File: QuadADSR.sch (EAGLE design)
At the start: 61 parts, among them IC1 74AC32D, IC5 MCP6004D, Q1 20MHz, T1 2N3904, T2 2N3904, T3 2N3904, T4 2N3904, U1 ATMEGA328P, U2 DUAL_OPAMP, U3 7805

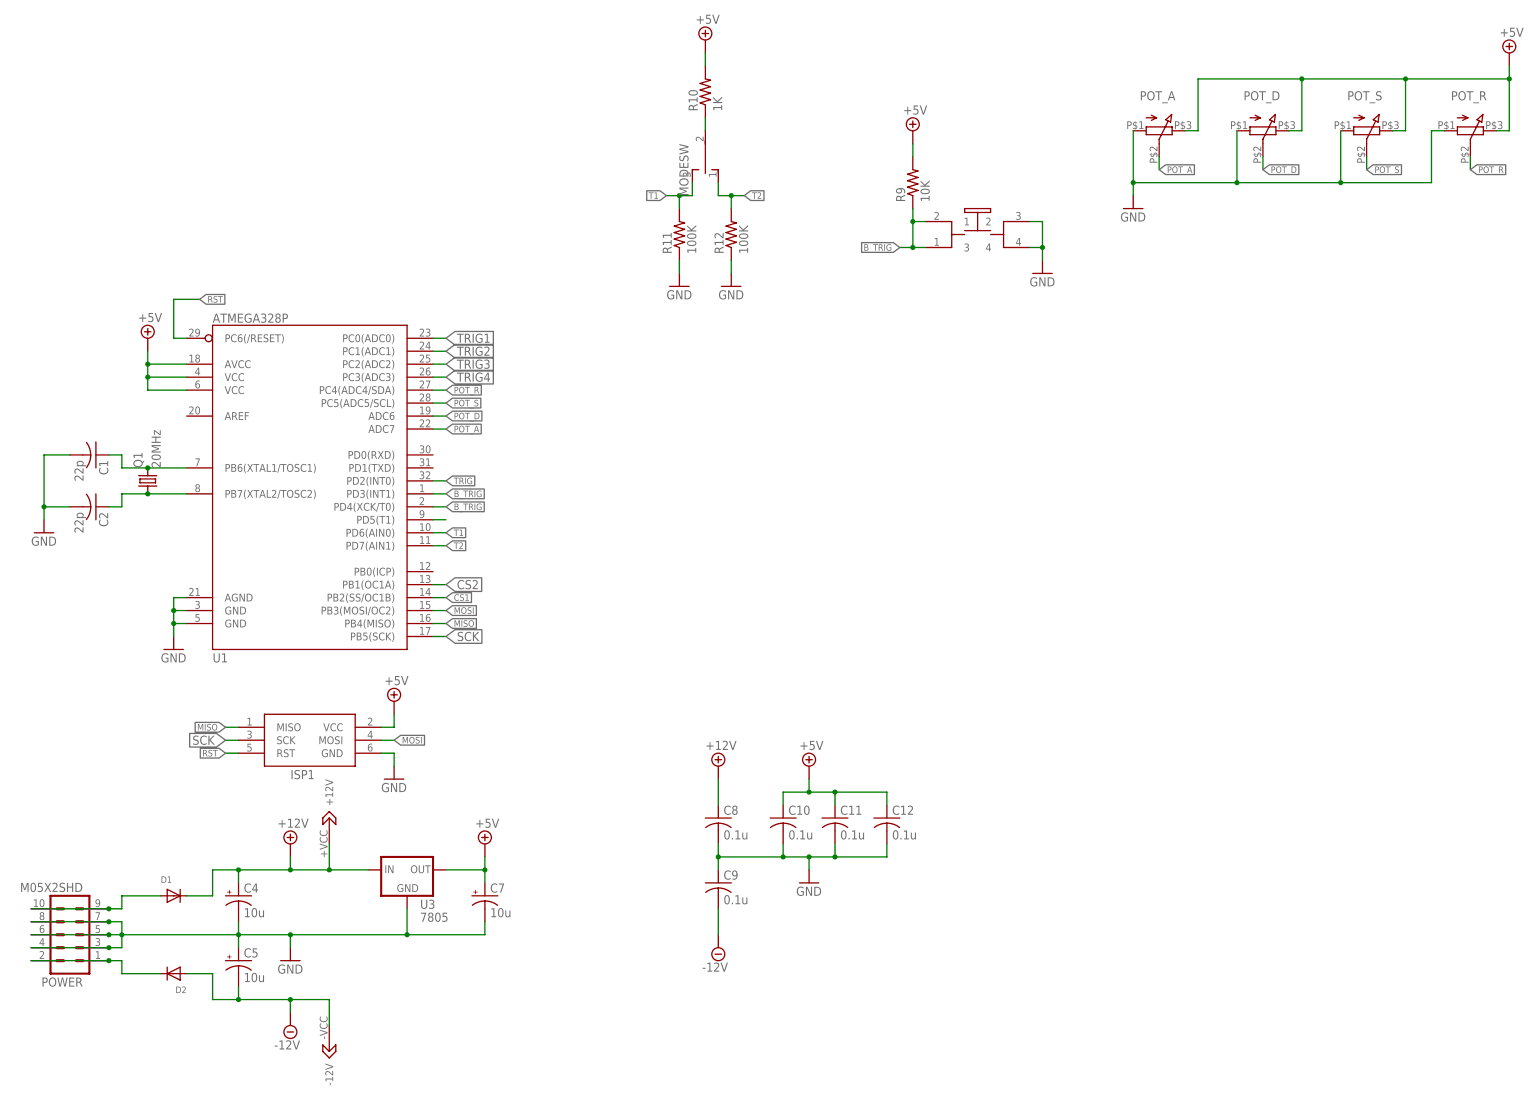
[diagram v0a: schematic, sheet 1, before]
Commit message: Layed out board with shape pots
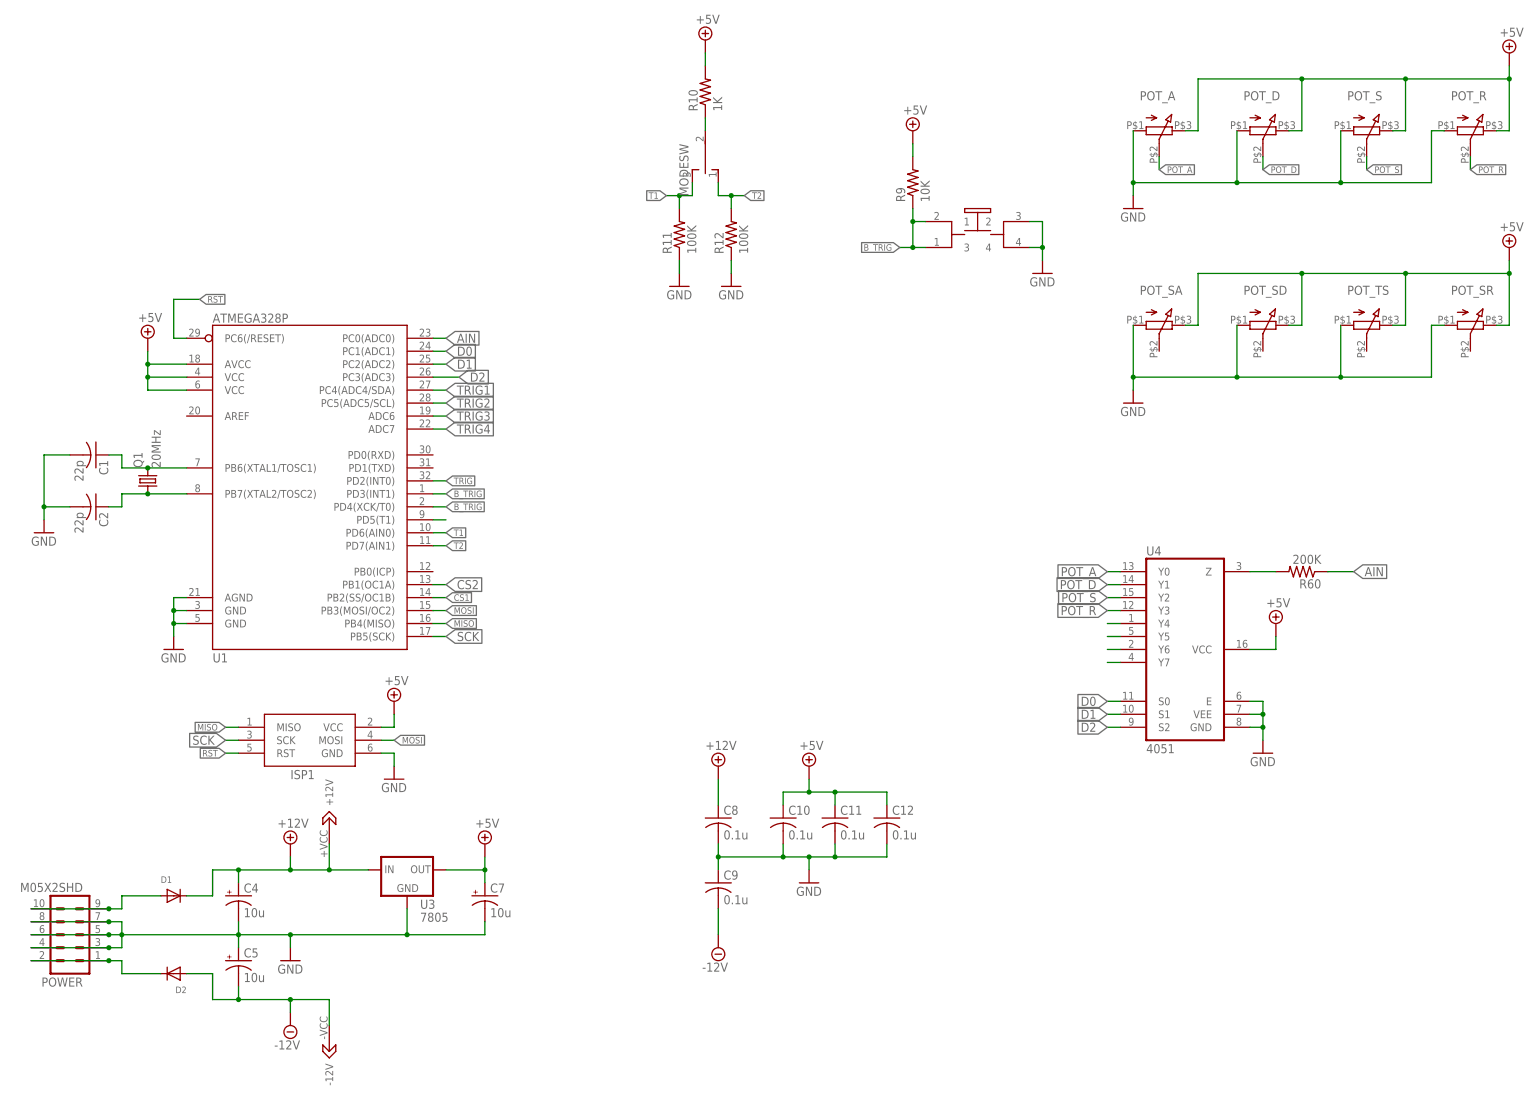
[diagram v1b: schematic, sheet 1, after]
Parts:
- added POT_SA, POT_SD, POT_SR, POT_TS: Q-POT, INSTRUO:Q-POT
- added R60: 200K, rcl:R-US_R0805
- added U4: 4051, INSTRUO:MUX!
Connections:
- new net AIN: R60.1, U1.PC0(ADC0)
- new net D0: U1.PC1(ADC1), U4.S0
- new net D1: U1.PC2(ADC2), U4.S1
- new net D2: U1.PC3(ADC3), U4.S2
- new net N$23: U4.Y4
- new net N$24: U4.Y5
- new net N$26: U4.Y6
- new net N$27: U4.Y7
- new net N$69: R60.2, U4.Z
- net +5V: now also POT_SA.3, POT_SD.3, POT_SR.3, POT_TS.3, U4.VCC
- net GND: now also POT_SA.1, POT_SD.1, POT_SR.1, POT_TS.1, U4.E, U4.GND, U4.VEE
- net POT_A: now also U4.Y0
- net POT_D: now also U4.Y1
- net POT_R: now also U4.Y3
- net POT_S: now also U4.Y2
- net TRIG1: now also U1.PC4(ADC4/SDA); no longer U1.PC0(ADC0)
- net TRIG2: now also U1.PC5(ADC5/SCL); no longer U1.PC1(ADC1)
- net TRIG3: now also U1.ADC6; no longer U1.PC2(ADC2)
- net TRIG4: now also U1.ADC7; no longer U1.PC3(ADC3)

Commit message: Moved a few thigs round
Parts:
- removed BUT: PB6149L-5, INSTRUO:PB6149L-5
- removed POT_TS: Q-POT, INSTRUO:Q-POT
- added D3: Red, led:LED5MM
- added D4: Green, led:LED5MM
- added D5: BLue, led:LED5MM
- added D6: Yellow, led:LED5MM
- added POT_ST: Q-POT, INSTRUO:Q-POT
- added R17, R18, R19: (no value), resistor:R-EU_R0805
- R9: value 10K -> (none); device rcl:R-US_R0805 -> resistor:R-EU_R0805
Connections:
- removed net B_TRIG: BUTG$1.1, BUTG$1.3, R9.1, U1.PD3(INT1), U1.PD4(XCK/T0)
- removed net D0: U1.PC1(ADC1), U4.S0
- removed net D1: U1.PC2(ADC2), U4.S1
- removed net D2: U1.PC3(ADC3), U4.S2
- removed net N$23: U4.Y4
- removed net N$24: U4.Y5
- removed net N$26: U4.Y6
- removed net N$27: U4.Y7
- new net LED_A: R9.2, U1.PD0(RXD)
- new net LED_B: R17.2, U1.PD1(TXD)
- new net LED_C: R18.2, U1.PD3(INT1)
- new net LED_D: R19.2, U1.PD4(XCK/T0)
- new net N$19: D3.A, R9.1
- new net N$20: D4.A, R17.1
- new net N$21: D5.A, R18.1
- new net N$22: D6.A, R19.1
- new net POT_SA: POT_SA.2, U4.Y4
- new net POT_SD: POT_SD.2, U4.Y5
- new net POT_SR: POT_SR.2, U4.Y7
- new net POT_ST: POT_ST.2, U4.Y6
- new net S0: U1.PC0(ADC0), U4.S0
- new net S1: U1.PC1(ADC1), U4.S1
- new net S2: U1.PC2(ADC2), U4.S2
- net +5V: now also POT_ST.3; no longer POT_TS.3, R9.2
- net AIN: now also U1.PC3(ADC3); no longer U1.PC0(ADC0)
- net GND: now also D3.C, D4.C, D5.C, D6.C, POT_ST.1; no longer BUTG$1.2, BUTG$1.4, POT_TS.1
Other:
- moved on the sheet: POT_SA, POT_SD, POT_SR, R60, U4

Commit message: Moved a few thigs round
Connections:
- removed net 3VREF: U$3.VREFA, U$3.VREFB, U$4.VREFA, U$4.VREFB
- removed net N$16: IC1P.GND
- removed net N$17: IC1P.VCC
- net +5V: now also C15.1, IC1P.VCC, IC5P.V+, U$3.VDD, U$3.VREFA, U$3.VREFB, U$4.VDD, U$4.VREFA, U$4.VREFB, U$4.~SHDN
- net 5V: no longer C15.1, IC5P.V+, U$3.VDD, U$4.VDD, U$4.~SHDN
- net GND: now also IC1P.GND
- net TRIG: no longer U1.PD5(T1)
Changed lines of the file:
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@@
 <part name="SUPPLY17" library="supply2" deviceset="+5V" device=""/>
 <part name="R60" library="rcl" deviceset="R-US_" device="R0805" value="200K"/>
+<part name="SUPPLY18" library="supply2" library_urn="urn:adsk.eagle:library:372" deviceset="+5V" device=""/>
+<part name="SUPPLY19" library="supply2" library_urn="urn:adsk.eagle:library:372" deviceset="+5V" device=""/>
+<part name="SUPPLY20" library="supply2" library_urn="urn:adsk.eagle:library:372" deviceset="+5V" device=""/>
+<part name="SUPPLY21" library="supply2" library_urn="urn:adsk.eagle:library:372" deviceset="+5V" device=""/>
+<part name="SUPPLY22" library="supply2" library_urn="urn:adsk.eagle:library:372" deviceset="+5V" device=""/>
+<part name="SUPPLY23" library="supply2" library_urn="urn:adsk.eagle:library:372" deviceset="+5V" device=""/>
 </parts>
 <sheets>
@@
 <junction x="25.4" y="-27.94"/>
 <pinref part="U3" gate="G$1" pin="GND"/>
-<wire x1="60.96" y1="-25.4" x2="83.82" y2="-25.4" width="0.1524" layer="91"/>
+<wire x1="60.96" y1="-25.4" x2="71.12" y2="-25.4" width="0.1524" layer="91"/>
+<wire x1="71.12" y1="-25.4" x2="83.82" y2="-25.4" width="0.1524" layer="91"/>
 <wire x1="83.82" y1="-25.4" x2="83.82" y2="-20.32" width="0.1524" layer="91"/>
 <junction x="60.96" y="-25.4"/>
@@
 <wire x1="99.06" y1="-25.4" x2="99.06" y2="-22.86" width="0.1524" layer="91"/>
 <junction x="83.82" y="-25.4"/>
+<wire x1="71.12" y1="-25.4" x2="71.12" y2="-30.48" width="0.1524" layer="91"/>
+<junction x="71.12" y="-25.4"/>
+<label x="73.66" y="-30.48" size="1.778" layer="95"/>
 </segment>
 <segment>
@@
 <wire x1="99.06" y1="-10.16" x2="99.06" y2="-12.7" width="0.1524" layer="91"/>
 <junction x="99.06" y="-12.7"/>
+<wire x1="99.06" y1="-12.7" x2="104.14" y2="-12.7" width="0.1524" layer="91"/>
+<label x="106.68" y="-12.7" size="1.778" layer="95"/>
 </segment>
 <segment>
@@
 </net>
 <net name="TRIG" class="0">
-<segment>
-<pinref part="U1" gate="G$1" pin="PD5(T1)"/>
-<wire x1="88.9" y1="55.88" x2="91.44" y2="55.88" width="0.1524" layer="91"/>
-</segment>
 <segment>
 <pinref part="U1" gate="G$1" pin="PD2(INT0)"/>
@@
 <instance part="C16" gate="G$1" x="7.62" y="71.12"/>
 <instance part="C17" gate="G$1" x="17.78" y="71.12"/>
+<instance part="SUPPLY18" gate="+5V" x="-10.16" y="124.46"/>
+<instance part="SUPPLY19" gate="+5V" x="35.56" y="124.46"/>
+<instance part="SUPPLY20" gate="+5V" x="38.1" y="124.46"/>
+<instance part="SUPPLY21" gate="+5V" x="-10.16" y="30.48"/>
+<instance part="SUPPLY22" gate="+5V" x="35.56" y="30.48"/>
+<instance part="SUPPLY23" gate="+5V" x="40.64" y="30.48"/>
 </instances>
 <busses>
@@
 </segment>
 <segment>
-<pinref part="C15" gate="G$1" pin="1"/>
-<pinref part="IC5" gate="P" pin="V+"/>
-<wire x1="93.98" y1="78.74" x2="86.36" y2="78.74" width="0.1524" layer="91"/>
-<wire x1="86.36" y1="78.74" x2="86.36" y2="81.28" width="0.1524" layer="91"/>
-<junction x="86.36" y="78.74"/>
-<label x="86.36" y="81.28" size="1.778" layer="95"/>
-</segment>
-<segment>
-<pinref part="U$3" gate="G$1" pin="VDD"/>
-<wire x1="-5.08" y1="119.38" x2="-10.16" y2="119.38" width="0.1524" layer="91"/>
-<label x="-10.16" y="119.38" size="1.778" layer="95" rot="R180"/>
-</segment>
-<segment>
 <pinref part="C16" gate="G$1" pin="1"/>
 <wire x1="7.62" y1="73.66" x2="7.62" y2="76.2" width="0.1524" layer="91"/>
@@
 </segment>
 <segment>
-<pinref part="U$4" gate="G$1" pin="VDD"/>
-<wire x1="-5.08" y1="25.4" x2="-10.16" y2="25.4" width="0.1524" layer="91"/>
-<label x="-10.16" y="25.4" size="1.778" layer="95" rot="R180"/>
-</segment>
-<segment>
 <pinref part="U$3" gate="G$1" pin="~SHDN"/>
 <wire x1="-5.08" y1="104.14" x2="-10.16" y2="104.14" width="0.1524" layer="91"/>
 <label x="-10.16" y="104.14" size="1.778" layer="95" rot="R180"/>
-</segment>
-<segment>
-<pinref part="U$4" gate="G$1" pin="~SHDN"/>
-<wire x1="-5.08" y1="10.16" x2="-10.16" y2="10.16" width="0.1524" layer="91"/>
-<label x="-10.16" y="10.16" size="1.778" layer="95" rot="R180"/>
 </segment>
 </net>
@@
 </segment>
 </net>
-<net name="3VREF" class="0">
+<net name="+5V" class="0">
+<segment>
+<pinref part="U$4" gate="G$1" pin="~SHDN"/>
+<wire x1="-5.08" y1="10.16" x2="-10.16" y2="10.16" width="0.1524" layer="91"/>
+<label x="-10.16" y="10.16" size="1.778" layer="95" rot="R180"/>
+</segment>
+<segment>
+<pinref part="C15" gate="G$1" pin="1"/>
+<pinref part="IC5" gate="P" pin="V+"/>
+<wire x1="93.98" y1="78.74" x2="86.36" y2="78.74" width="0.1524" layer="91"/>
+<wire x1="86.36" y1="78.74" x2="86.36" y2="81.28" width="0.1524" layer="91"/>
+<junction x="86.36" y="78.74"/>
+<label x="86.36" y="81.28" size="1.778" layer="95"/>
+</segment>
 <segment>
 <pinref part="U$3" gate="G$1" pin="VREFA"/>
 <wire x1="30.48" y1="119.38" x2="35.56" y2="119.38" width="0.1524" layer="91"/>
-<label x="35.56" y="119.38" size="1.778" layer="95"/>
+<pinref part="SUPPLY19" gate="+5V" pin="+5V"/>
+<wire x1="35.56" y1="119.38" x2="35.56" y2="121.92" width="0.1524" layer="91"/>
 </segment>
 <segment>
 <pinref part="U$3" gate="G$1" pin="VREFB"/>
-<wire x1="30.48" y1="116.84" x2="35.56" y2="116.84" width="0.1524" layer="91"/>
-<label x="35.56" y="116.84" size="1.778" layer="95"/>
+<wire x1="30.48" y1="116.84" x2="38.1" y2="116.84" width="0.1524" layer="91"/>
+<pinref part="SUPPLY20" gate="+5V" pin="+5V"/>
+<wire x1="38.1" y1="116.84" x2="38.1" y2="121.92" width="0.1524" layer="91"/>
+</segment>
+<segment>
+<pinref part="SUPPLY18" gate="+5V" pin="+5V"/>
+<wire x1="-10.16" y1="121.92" x2="-10.16" y2="119.38" width="0.1524" layer="91"/>
+<pinref part="U$3" gate="G$1" pin="VDD"/>
+<wire x1="-10.16" y1="119.38" x2="-5.08" y2="119.38" width="0.1524" layer="91"/>
+</segment>
+<segment>
+<pinref part="U$4" gate="G$1" pin="VDD"/>
+<wire x1="-5.08" y1="25.4" x2="-10.16" y2="25.4" width="0.1524" layer="91"/>
+<pinref part="SUPPLY21" gate="+5V" pin="+5V"/>
+<wire x1="-10.16" y1="25.4" x2="-10.16" y2="27.94" width="0.1524" layer="91"/>
 </segment>
 <segment>
 <pinref part="U$4" gate="G$1" pin="VREFA"/>
 <wire x1="30.48" y1="25.4" x2="35.56" y2="25.4" width="0.1524" layer="91"/>
-<label x="35.56" y="25.4" size="1.778" layer="95"/>
+<pinref part="SUPPLY22" gate="+5V" pin="+5V"/>
+<wire x1="35.56" y1="25.4" x2="35.56" y2="27.94" width="0.1524" layer="91"/>
 </segment>
 <segment>
 <pinref part="U$4" gate="G$1" pin="VREFB"/>
-<wire x1="30.48" y1="22.86" x2="35.56" y2="22.86" width="0.1524" layer="91"/>
-<label x="35.56" y="22.86" size="1.778" layer="95"/>
+<wire x1="30.48" y1="22.86" x2="40.64" y2="22.86" width="0.1524" layer="91"/>
+<pinref part="SUPPLY23" gate="+5V" pin="+5V"/>
+<wire x1="40.64" y1="22.86" x2="40.64" y2="27.94" width="0.1524" layer="91"/>
 </segment>
 </net>
@@
 <pinref part="GND21" gate="1" pin="GND"/>
 </segment>
+<segment>
+<pinref part="IC1" gate="P" pin="GND"/>
+<pinref part="GND22" gate="1" pin="GND"/>
+<wire x1="-40.64" y1="53.34" x2="-40.64" y2="50.8" width="0.1524" layer="91"/>
+</segment>
 </net>
 <net name="+5V" class="0">
@@
 <pinref part="SUPPLY15" gate="+5V" pin="+5V"/>
 <wire x1="101.6" y1="10.16" x2="101.6" y2="7.62" width="0.1524" layer="91"/>
+</segment>
+<segment>
+<pinref part="IC1" gate="P" pin="VCC"/>
+<pinref part="SUPPLY16" gate="+5V" pin="+5V"/>
+<wire x1="-40.64" y1="68.58" x2="-40.64" y2="71.12" width="0.1524" layer="91"/>
 </segment>
 </net>
@@
 </segment>
 </net>
-<net name="N$16" class="0">
-<segment>
-<pinref part="IC1" gate="P" pin="GND"/>
-<wire x1="-40.64" y1="53.34" x2="-40.64" y2="50.8" width="0.1524" layer="91"/>
-</segment>
-</net>
-<net name="N$17" class="0">
-<segment>
-<pinref part="IC1" gate="P" pin="VCC"/>
-<wire x1="-40.64" y1="68.58" x2="-40.64" y2="71.12" width="0.1524" layer="91"/>
-</segment>
-</net>
